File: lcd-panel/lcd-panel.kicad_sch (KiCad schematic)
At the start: 27 parts, among them J1 USB wire, J2 LCD FPC connector, J3 Fan Socket, Q1 AO3400A, U1 FT232HL-REEL, U2 93LC56BT-I/OT, U3 USBLC6-2SC6, Y1 12 MHz, 20 pF load, ±10 ppm

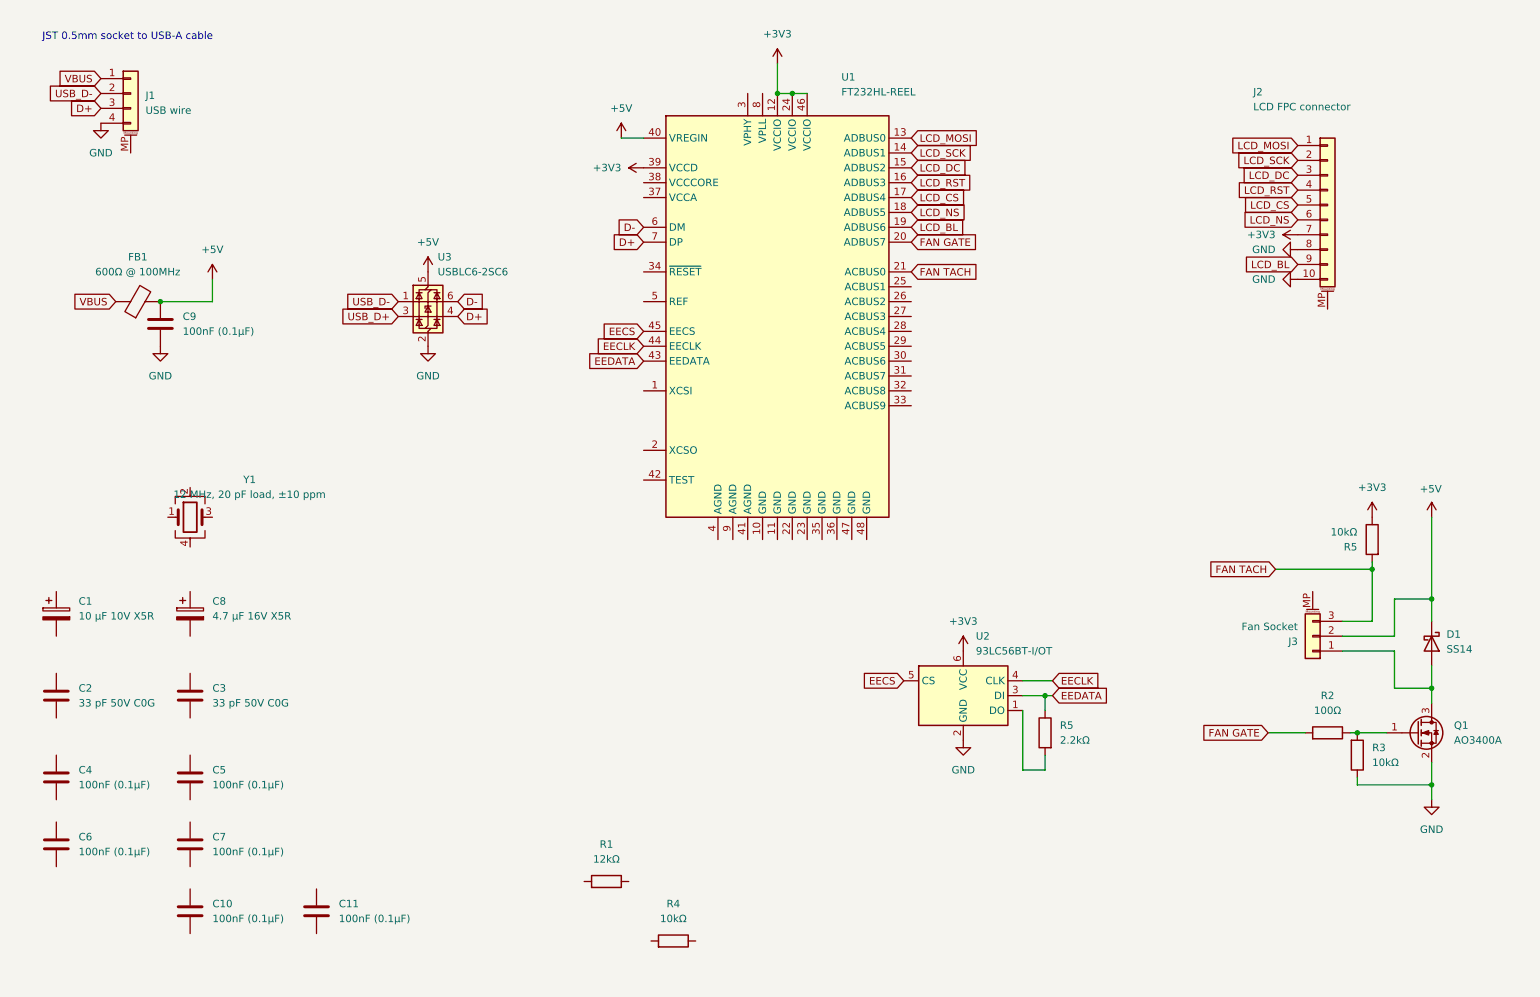
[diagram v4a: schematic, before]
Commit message: Hooking up the crystal clock
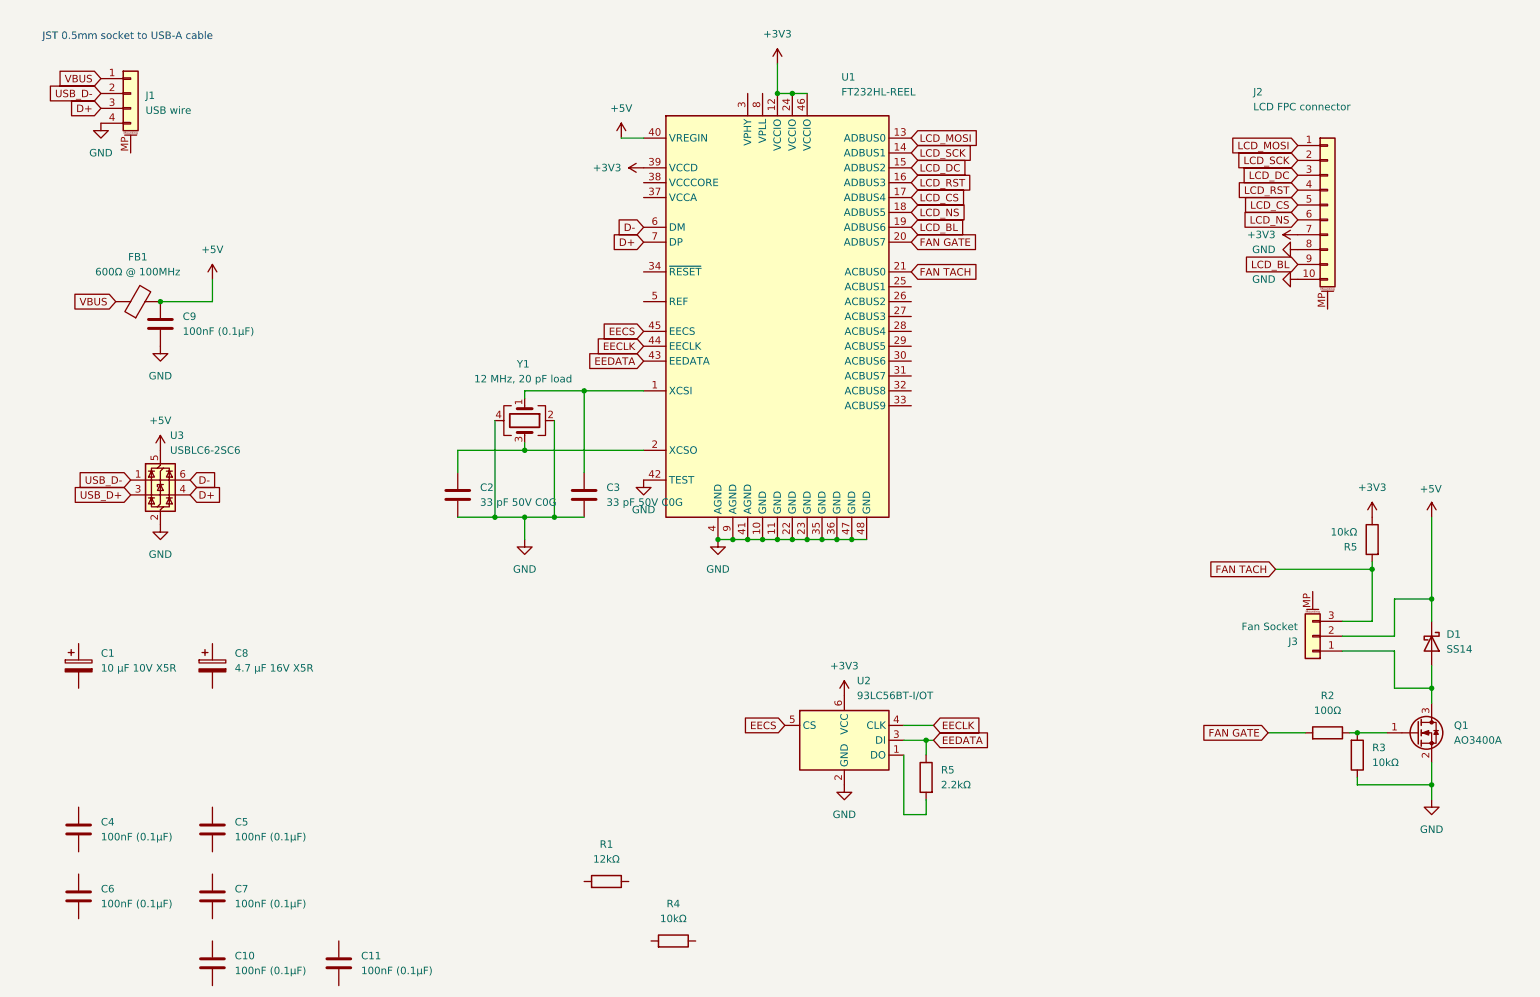
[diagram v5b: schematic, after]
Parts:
- Y1: value 12 MHz, 20 pF load, ±10 ppm -> 12 MHz, 20 pF load
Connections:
- net GND: now also C2.2, C3.2, U1.10 (GND), U1.11 (GND), U1.22 (GND), U1.23 (GND), U1.35 (GND), U1.36 (GND), U1.4 (AGND), U1.41 (AGND), U1.42 (TEST), U1.47 (GND), U1.48 (GND), U1.9 (AGND), Y1.2, Y1.4
- net at U1.1 (XCSI): now also C3.1, Y1.1
- net at U1.2 (XCSO): now also C2.1, Y1.3
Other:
- moved on the sheet: C1, C10, C11, C2, C3, C4, C5, C6, C7, C8, R5, U2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

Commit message: Filling up the rest of the schematic
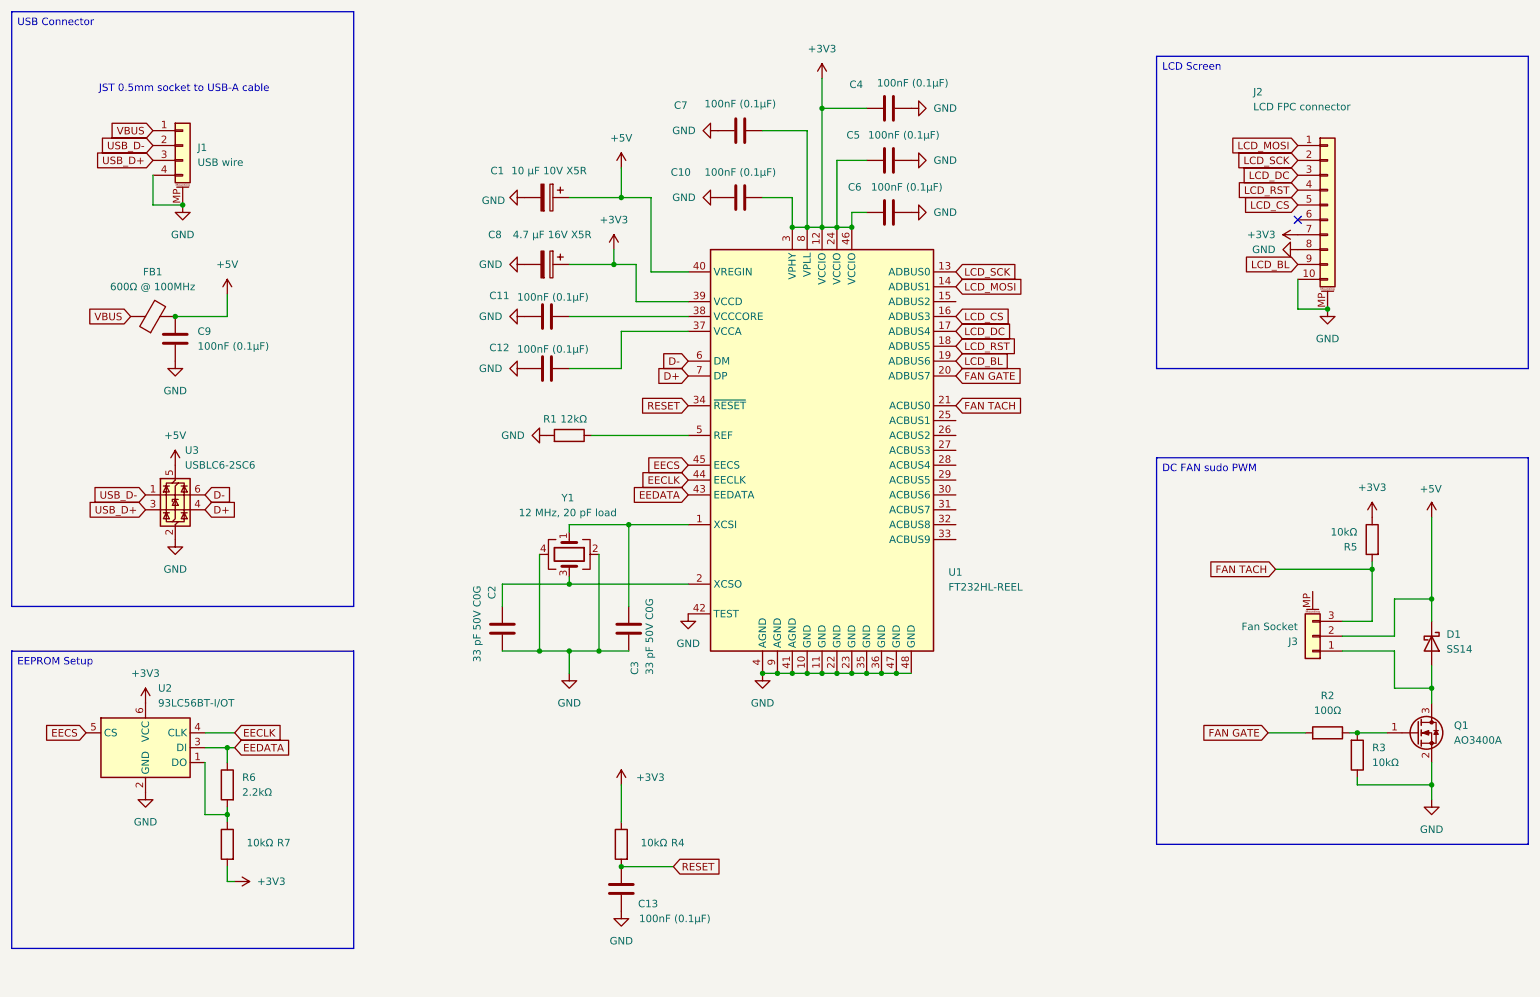
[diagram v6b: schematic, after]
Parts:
- added C12, C13: 100nF (0.1µF), Capacitor_SMD:C_0402_1005Metric, symbol PCM_Capacitor_US_AKL:C_Generic
- added R7: 10kΩ, Resistor_SMD:R_0402_1005Metric, symbol PCM_Resistor_AKL:R_0603
- renumbered R5 to R6
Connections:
- net +3V3: now also C10.2, C4.1, C5.1, C6.1, C7.2, C8.1, R4.2, U1.3 (VPHY), U1.8 (VPLL), R7.1
- net +5V: now also C1.1
- net D+: no longer J1.3 (Pin_3)
- net GND: now also C1.2, C10.1, C11.1, C4.2, C5.2, C6.2, C7.1, C8.2, J1.MP (MountPin), J2.MP (MountPin), R1.1, C12.1, C13.1
- net LCD_CS: now also U1.16 (ADBUS3); no longer U1.17 (ADBUS4)
- net LCD_DC: now also U1.17 (ADBUS4); no longer U1.15 (ADBUS2)
- net LCD_MOSI: now also U1.14 (ADBUS1); no longer U1.13 (ADBUS0)
- net LCD_RST: now also U1.18 (ADBUS5); no longer U1.16 (ADBUS3)
- net LCD_SCK: now also U1.13 (ADBUS0); no longer U1.14 (ADBUS1)
- net USB_D+: now also J1.3 (Pin_3)
- net RESET: now reaches R4.1
- net RESET: now also U1.34 (~{RESET}), C13.2
- net at U1.37 (VCCA): now also C12.2
- net at U1.38 (VCCCORE): now also C11.2
- net at U1.5 (REF): now also R1.2
- net at R6.1, U2.1 (DO): now also R7.2
- net LCD_NS: no longer names the net of J2.6 (Pin_6)
- net LCD_NS: no longer U1.18 (ADBUS5)
- no-connect marks 0 -> 1
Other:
- moved on the sheet: C1, C10, C11, C2, C3, C4, C5, C6, C7, C8, C9, FB1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

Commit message: Hooking up most of the wiring
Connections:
- net FAN TACH: now also U1.25 (ACBUS1); no longer U1.21 (ACBUS0)
- net GND: now also J3.MP (MountPin)
- net LCD_BL: now also U1.17 (ADBUS4); no longer U1.19 (ADBUS6)
- net LCD_DC: now also U1.19 (ADBUS6); no longer U1.17 (ADBUS4)

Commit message: Fine tuning the BOM for JLCPCBA components
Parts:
- J1: LCSC C293774 -> C116890
- J2: LCSC C466531 -> C506791
- J3: LCSC C293773 -> C88352
- R6: LCSC C25744 -> C25879
- U2: LCSC C135111 -> C190271
- U3: LCSC (none) -> C7519
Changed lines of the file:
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@@
 			)
 		)
+		(property "LCSC" "C7519"
+			(at 45.72 100.33 0)
+			(effects
+				(font
+					(size 1.27 1.27)
+				)
+				(hide yes)
+			)
+		)
 		(pin "6"
 		)
@@
 			)
 		)
-		(property "LCSC" "C135111"
+		(property "LCSC" "C190271"
 			(at 40.64 143.51 0)
 			(effects
@@
 			)
 		)
-		(property "LCSC" "C466531"
+		(property "LCSC" "C506791"
 			(at 242.57 50.8 0)
 			(effects
@@
 			)
 		)
-		(property "LCSC" "C293773"
+		(property "LCSC" "C88352"
 			(at 240.03 124.46 0)
 			(effects
@@
 			)
 		)
-		(property "LCSC" "C293774"
+		(property "LCSC" " C116890"
 			(at 46.99 40.64 0)
 			(effects
@@
 			)
 		)
-		(property "LCSC" "C25744"
+		(property "LCSC" "C25879"
 			(at 54.61 149.86 90)
 			(effects
